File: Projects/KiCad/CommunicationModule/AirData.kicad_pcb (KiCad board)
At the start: 2 copper layers, 110 x 95 mm, 34 parts, among them J1 Conn_01x08, SW1 SW_Push, U1 MCP2562-E-P, U2 MCP2515-I/P, U3 NJM7805SDL1, U4 ABX00012, Y1 8MHz

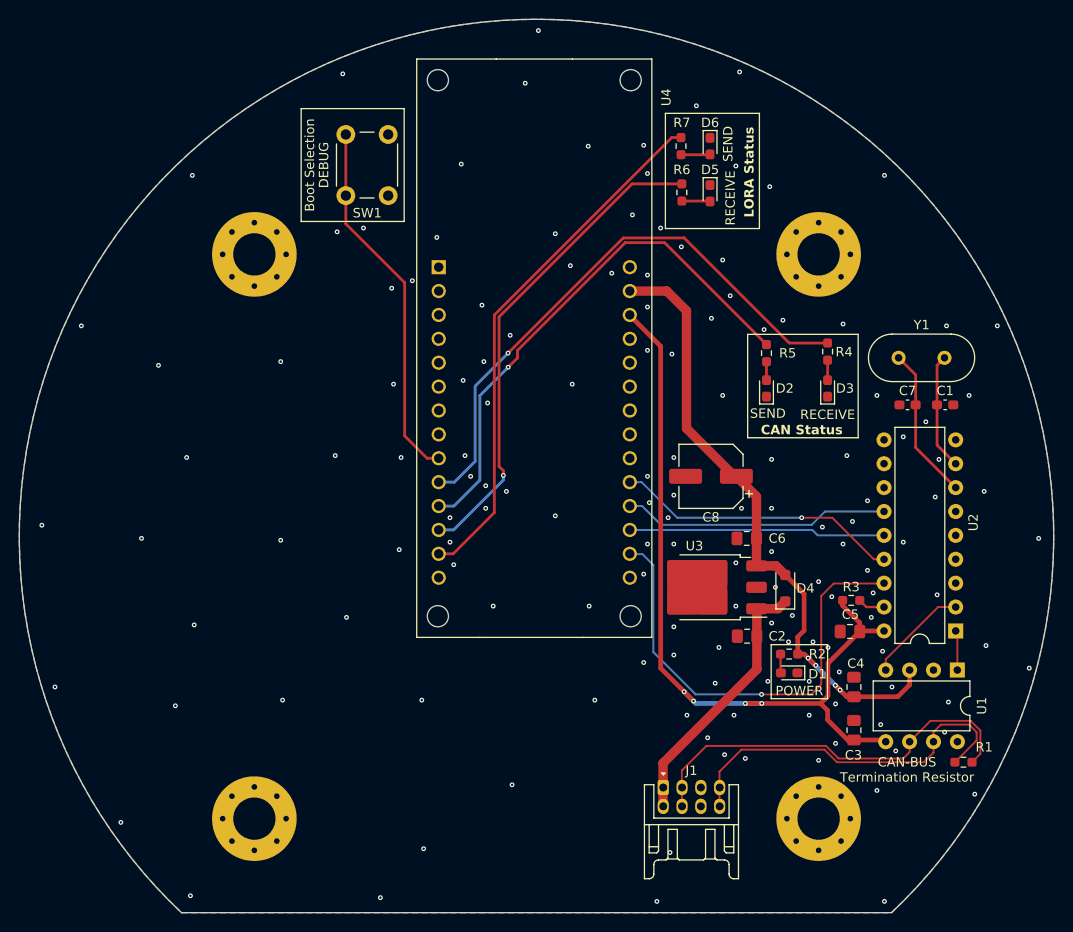
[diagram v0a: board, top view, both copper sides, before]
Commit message: 穴径を調整
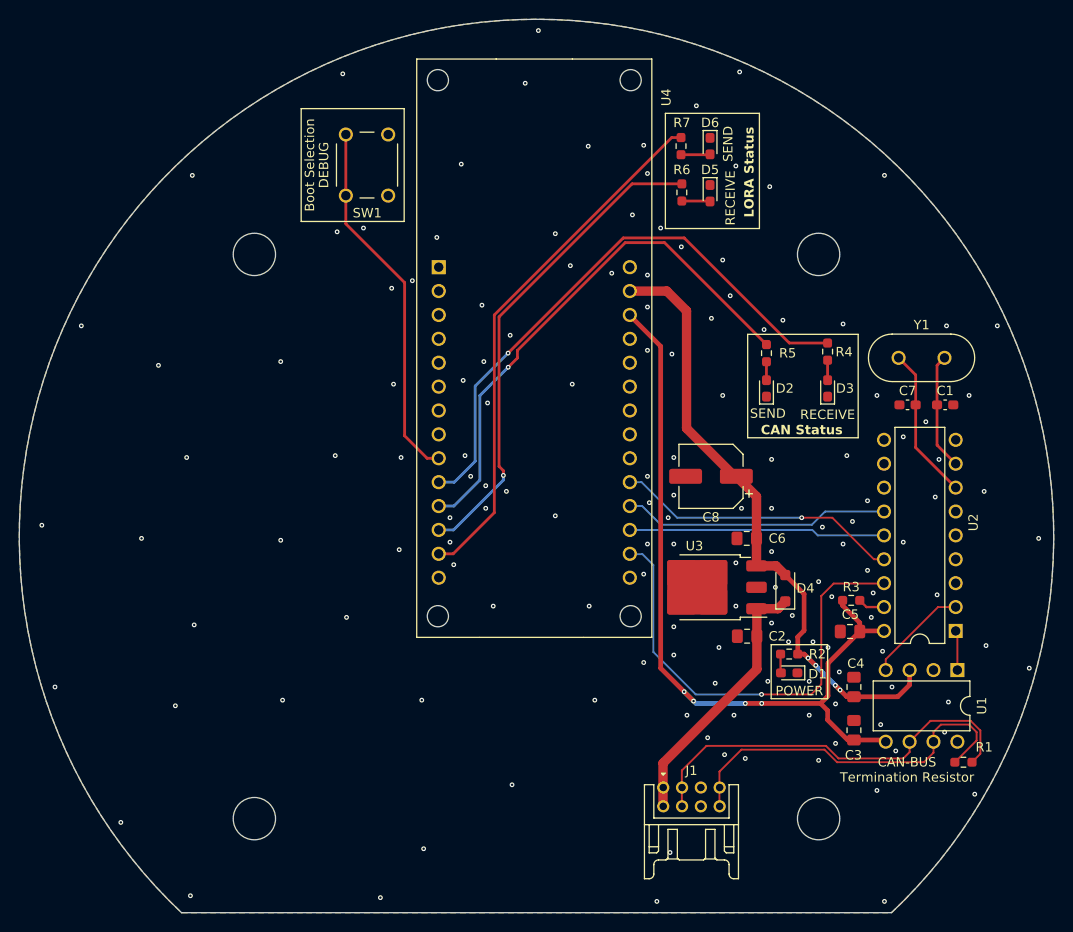
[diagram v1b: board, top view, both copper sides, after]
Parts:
- REF** (x4): value MountingHole_4.5mm_Pad_Via -> MountingHole_4.5mm; footprint MountingHole:MountingHole_4.5mm_Pad_Via -> MountingHole:MountingHole_4.5mm

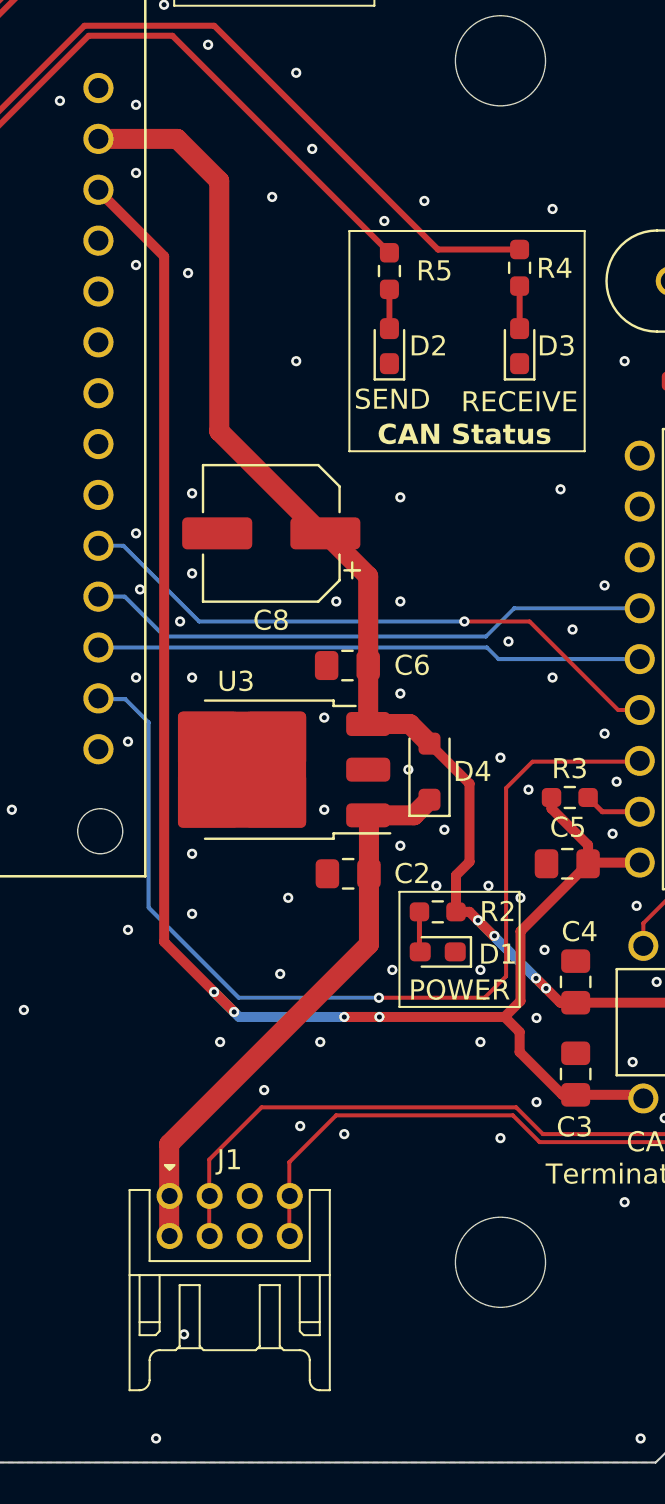
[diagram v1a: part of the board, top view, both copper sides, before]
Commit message: テストポイントを追加
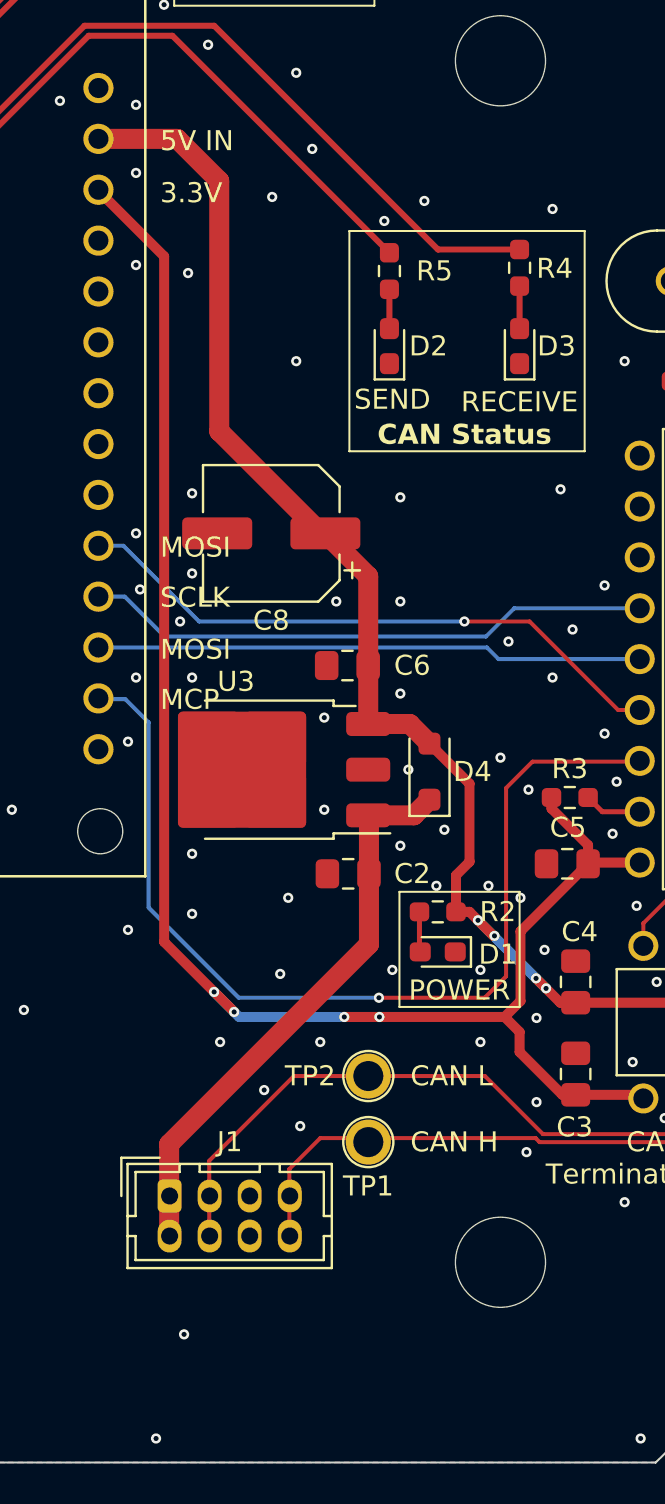
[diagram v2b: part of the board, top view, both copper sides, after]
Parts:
- added TP1: TestPoint, Connector_Pin:Pin_D1.0mm_L10.0mm, F.Cu at (171.9, 129.0)
- added TP2: TestPoint, Connector_Pin:Pin_D1.0mm_L10.0mm, F.Cu at (171.9, 125.7)
- J1: footprint Hirose_Connector:Hirose_DF11B-8DP-2DS -> Connector_Hirose:Hirose_DF11-8DP-2DSA_2x04_P2.00mm_Vertical
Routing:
- net CAN_L: track 43.7 -> 44.9 mm
- net CAN_H: track 40.0 -> 38.8 mm
- net GND: vias 147 -> 146
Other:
- board text added: "3.3V"
- board text added: "5V IN"
- board text added: "CAN H"
- board text added: "CAN L"
- board text added: "MCP"
- board text added: "MOSI"
- board text added: "SCLK"

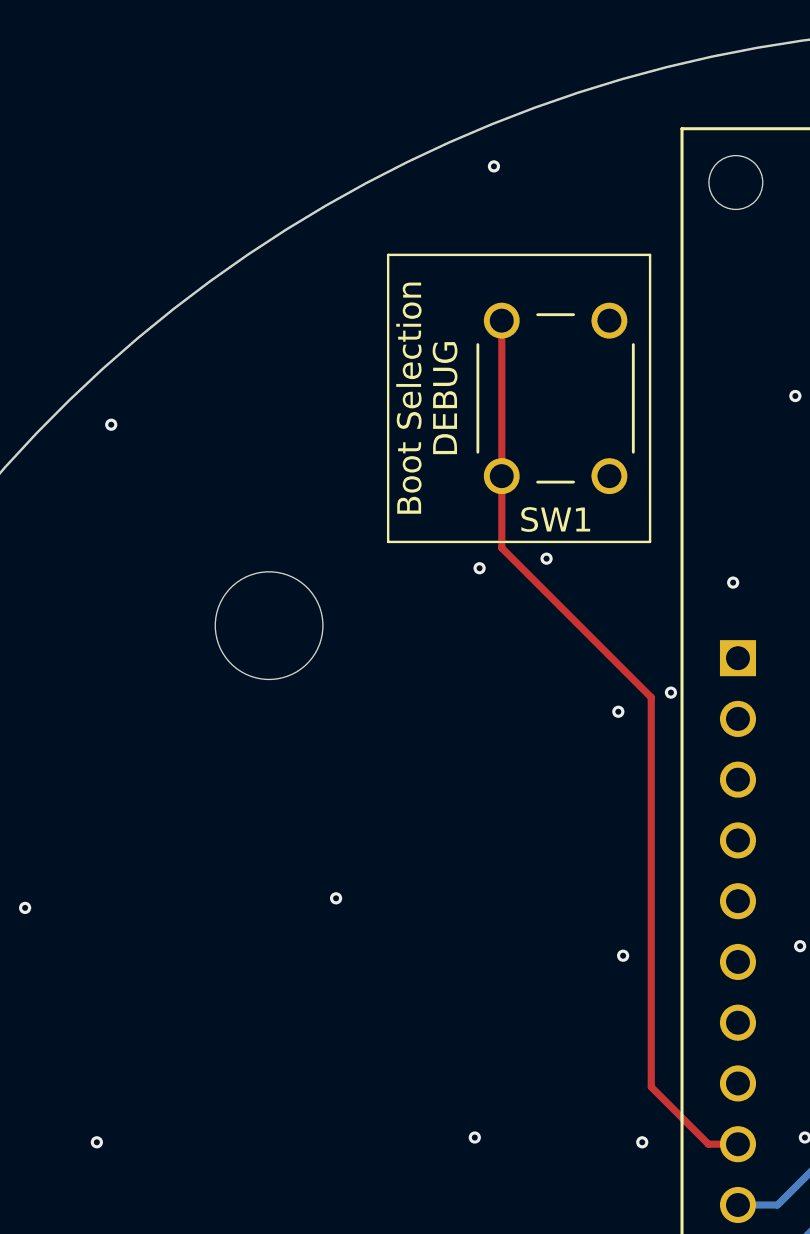
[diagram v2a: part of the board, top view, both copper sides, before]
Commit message: スイッチをピアノスイッチに変更
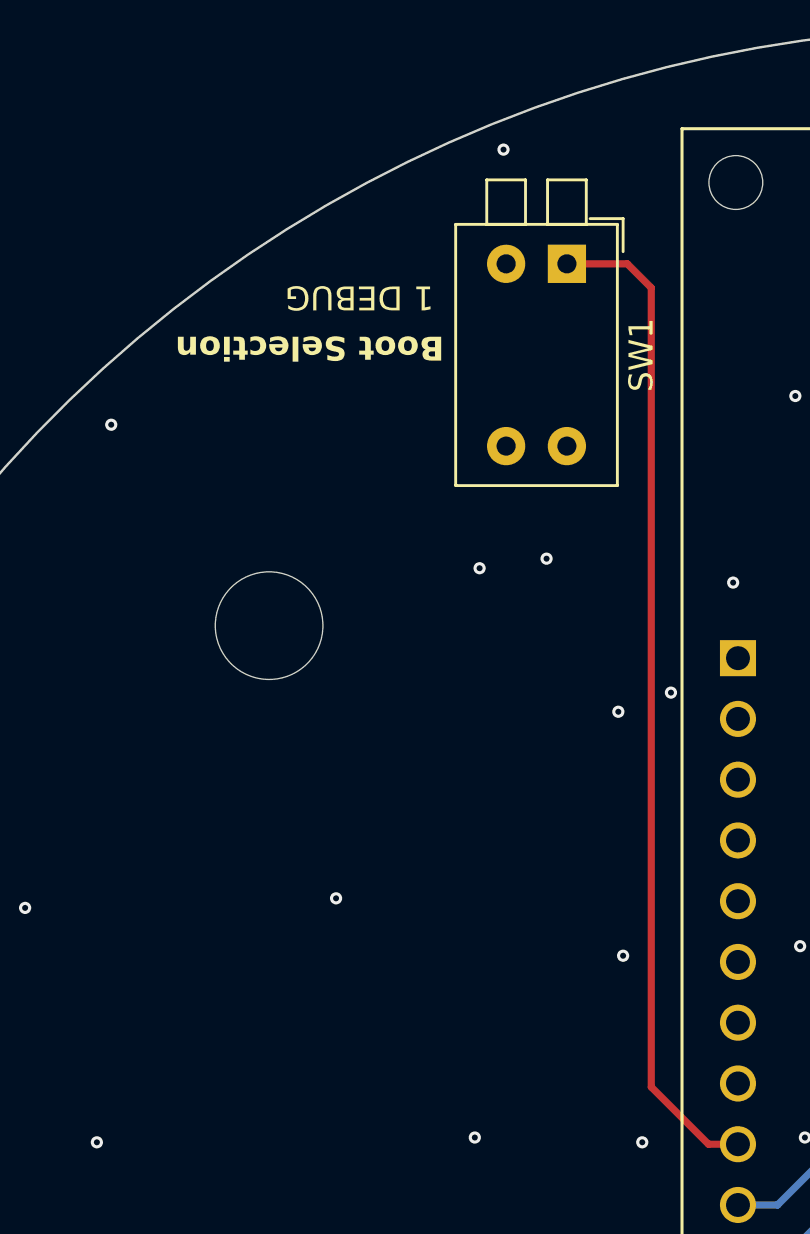
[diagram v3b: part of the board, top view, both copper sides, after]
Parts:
- SW1: value SW_Push -> SW_DIP_x02; footprint Button_Switch_THT:SW_PUSH_6mm -> Button_Switch_THT:SW_DIP_SPSTx02_Piano_10.8x6.64mm_W7.62mm_P2.54mm
- moved SW1 2.97 mm to (130.9, 59.9)
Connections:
- SW1 pad 1: GND -> DEBUG_MODE
- SW1 pad 2: DEBUG_MODE -> (no net)
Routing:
- net DEBUG_MODE: track 39.2 -> 41.9 mm
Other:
- board text added: "1 DEBUG"
- board text removed: "DEBUG"

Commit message: ベタを修正
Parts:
- moved C8 5.75 mm to (172.8, 98.6), turned to 0 degrees
- moved C6 2.04 mm to (171.2, 107.2)
- moved U3 1.55 mm to (167.3, 111.9)
- moved D4 1.42 mm to (175.2, 111.9)
- moved C2 1.35 mm to (170.8, 116.9)
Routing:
- net +5V: track 67.7 -> 70.8 mm
- net +12V: track 28.5 -> 27.1 mm
- net GND: vias 146 -> 136

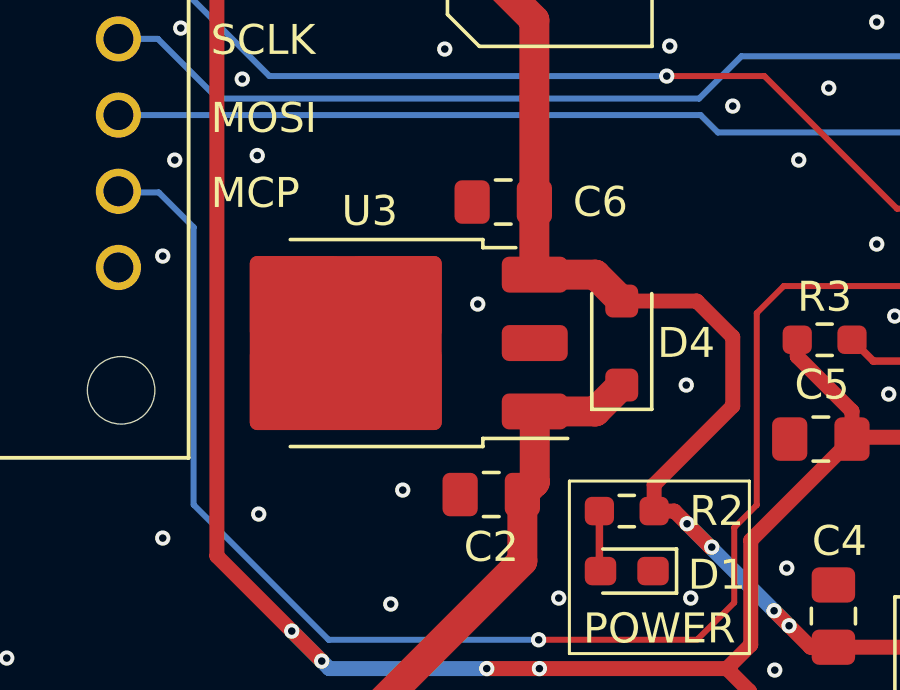
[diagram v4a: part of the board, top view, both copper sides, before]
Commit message: 三端子レギュレータをTO-252-3からTO-252-2に変更
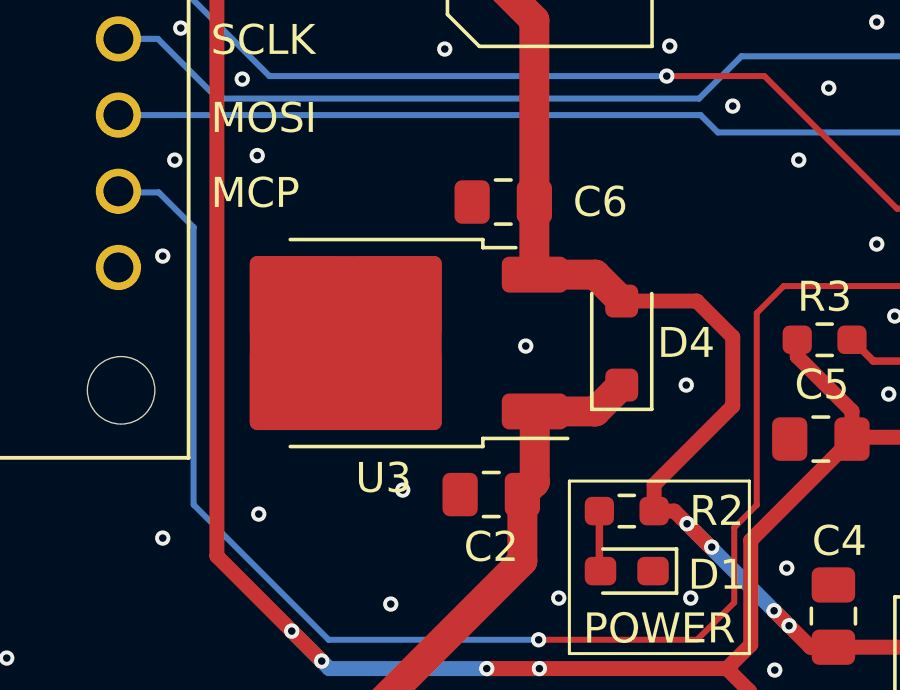
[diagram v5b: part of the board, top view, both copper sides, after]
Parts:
- U3: footprint Package_TO_SOT_SMD:TO-252-3_TabPin2 -> Package_TO_SOT_SMD:TO-252-2
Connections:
- SW1 pad 2: (no net) -> unconnected-(SW1-Pad2)
- SW1 pad 3: GND -> unconnected-(SW1-Pad3)
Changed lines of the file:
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@@
   (net 48 "unconnected-(U4-+5V-Pad28)")
   (net 49 "+12V")
+  (net 50 "unconnected-(SW1-Pad2)")
+  (net 51 "unconnected-(SW1-Pad3)")
   (footprint "MountingHole:MountingHole_4.5mm" locked (layer "F.Cu")
     (at 178.5 75)
@@
     (descr "2x-dip-switch SPST , Piano, row spacing 7.62 mm (300 mils), body size 10.8x6.64mm")
     (tags "DIP Switch SPST Piano 7.62mm 300mil")
-    (property "Sheetfile" "SensingModule.kicad_sch")
+    (property "Sheetfile" "AirData.kicad_sch")
     (property "Sheetname" "")
     (property "ki_description" "2x DIP Switch, Single Pole Single Throw (SPST) switch, small symbol")
@@
       (net 36 "DEBUG_MODE") (pintype "passive"))
     (pad "2" thru_hole oval (at 0 2.54 270) (size 1.6 1.6) (drill 0.8) (layers "*.Cu" "*.Mask")
-      (pintype "passive"))
+      (net 50 "unconnected-(SW1-Pad2)") (pintype "passive"))
     (pad "3" thru_hole oval (at 7.62 2.54 270) (size 1.6 1.6) (drill 0.8) (layers "*.Cu" "*.Mask")
-      (net 2 "GND") (pintype "passive"))
+      (net 51 "unconnected-(SW1-Pad3)") (pintype "passive"))
     (pad "4" thru_hole oval (at 7.62 0 270) (size 1.6 1.6) (drill 0.8) (layers "*.Cu" "*.Mask")
       (net 2 "GND") (pintype "passive"))
@@
     )
   )
-  (footprint "Package_TO_SOT_SMD:TO-252-3_TabPin2" (layer "F.Cu")
+  (footprint "Package_TO_SOT_SMD:TO-252-2" (layer "F.Cu")
     (at 167.26 111.899432 180)
     (descr "TO-252/DPAK SMD package, http://www.infineon.com/cms/en/product/packages/PG-TO252/PG-TO252-3-1/")
@@
     (property "ki_keywords" "Voltage Regulator 1.5A Positive")
     (attr smd)
-    (fp_text reference "U3" (at 0.46 4.4) (layer "F.SilkS")
+    (fp_text reference "U3" (at 0 -4.5 180) (layer "F.SilkS")
         (effects (font (size 1 1) (thickness 0.15)))
     )
-    (fp_text value "NJM7805SDL1" (at 0 4.5) (layer "F.Fab")
+    (fp_text value "NJM7805SDL1" (at 0 4.5 180) (layer "F.Fab")
         (effects (font (size 1 1) (thickness 0.15)))
     )
-    (fp_text user "${REFERENCE}" (at 0 0) (layer "F.Fab")
+    (fp_text user "${REFERENCE}" (at 0 0 180) (layer "F.Fab")
         (effects (font (size 1 1) (thickness 0.15)))
     )
@@
     (fp_line (start -5.81 -1.905) (end -3.11 -1.905)
       (stroke (width 0.1) (type solid)) (layer "F.Fab"))
-    (fp_line (start -5.81 -0.375) (end -5.81 0.375)
-      (stroke (width 0.1) (type solid)) (layer "F.Fab"))
-    (fp_line (start -5.81 0.375) (end -3.11 0.375)
-      (stroke (width 0.1) (type solid)) (layer "F.Fab"))
     (fp_line (start -5.81 1.905) (end -5.81 2.655)
       (stroke (width 0.1) (type solid)) (layer "F.Fab"))
@@
     (fp_line (start -3.11 -2.25) (end -2.11 -3.25)
       (stroke (width 0.1) (type solid)) (layer "F.Fab"))
-    (fp_line (start -3.11 -0.375) (end -5.81 -0.375)
-      (stroke (width 0.1) (type solid)) (layer "F.Fab"))
     (fp_line (start -3.11 1.905) (end -5.81 1.905)
       (stroke (width 0.1) (type solid)) (layer "F.Fab"))
@@
     (pad "1" smd roundrect (at -5.04 -2.28 180) (size 2.2 1.2) (layers "F.Cu" "F.Paste" "F.Mask") (roundrect_rratio 0.208333)
       (net 49 "+12V") (pinfunction "IN") (pintype "power_in"))
-    (pad "2" smd roundrect (at -5.04 0 180) (size 2.2 1.2) (layers "F.Cu" "F.Paste" "F.Mask") (roundrect_rratio 0.208333)
-      (net 2 "GND") (pinfunction "GND") (pintype "power_in"))
     (pad "2" smd roundrect (at -0.415 -1.525 180) (size 3.05 2.75) (layers "F.Cu" "F.Paste") (roundrect_rratio 0.090909)
       (net 2 "GND") (pinfunction "GND") (pintype "power_in"))
@@
     (pad "3" smd roundrect (at -5.04 2.28 180) (size 2.2 1.2) (layers "F.Cu" "F.Paste" "F.Mask") (roundrect_rratio 0.208333)
       (net 3 "+5V") (pinfunction "OUT") (pintype "power_out"))
-    (model "${KICAD6_3DMODEL_DIR}/Package_TO_SOT_SMD.3dshapes/TO-252-3_TabPin2.wrl"
+    (model "${KICAD6_3DMODEL_DIR}/Package_TO_SOT_SMD.3dshapes/TO-252-2.wrl"
       (offset (xyz 0 0 0))
       (scale (xyz 1 1 1))
@@
   (via (at 181.1 82.4) (size 0.51) (drill 0.25) (layers "F.Cu" "B.Cu") (free) (net 2))
   (via (at 128.3 113.6) (size 0.51) (drill 0.25) (layers "F.Cu" "B.Cu") (free) (net 2))
-  (via (at 170.4 110.599432) (size 0.51) (drill 0.25) (layers "F.Cu" "B.Cu") (free) (net 2))
+  (via (at 172 111.999432) (size 0.51) (drill 0.25) (layers "F.Cu" "B.Cu") (free) (net 2))
   (via (at 139.3 103) (size 0.51) (drill 0.25) (layers "F.Cu" "B.Cu") (free) (net 2))
   (via (at 177.5 124) (size 0.51) (drill 0.25) (layers "F.Cu" "B.Cu") (free) (net 2))
